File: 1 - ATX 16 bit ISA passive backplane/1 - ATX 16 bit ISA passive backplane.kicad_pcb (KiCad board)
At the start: 2 copper layers, 161.3 x 181.6 mm, 106 parts, among them J1 BUS 1, J10 AB15, J11 AB15, J12 AB15, J13 AB15, J14 AB15, J15 AB15, J16 AB15, J17 3.3V BYPASS, J18 ATX POWER, J19 -5V BYPASS, J2 BUS 2, J20 PWR SW, J21 RST POL, J22 ACT LED, J23 RST SW, J24 RST LED, J25 PWR LED, J3 BUS 3, J4 BUS 4, J5 BUS 5, J6 BUS 6, J7 BUS 7, J8 BREADBOARD HEADER (RC2014 COM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, J9 EXTENDED HEADER, SW1 POWER, SW2 RESET, U1 74HCT14, U2 LM7905, U3 74HCT74

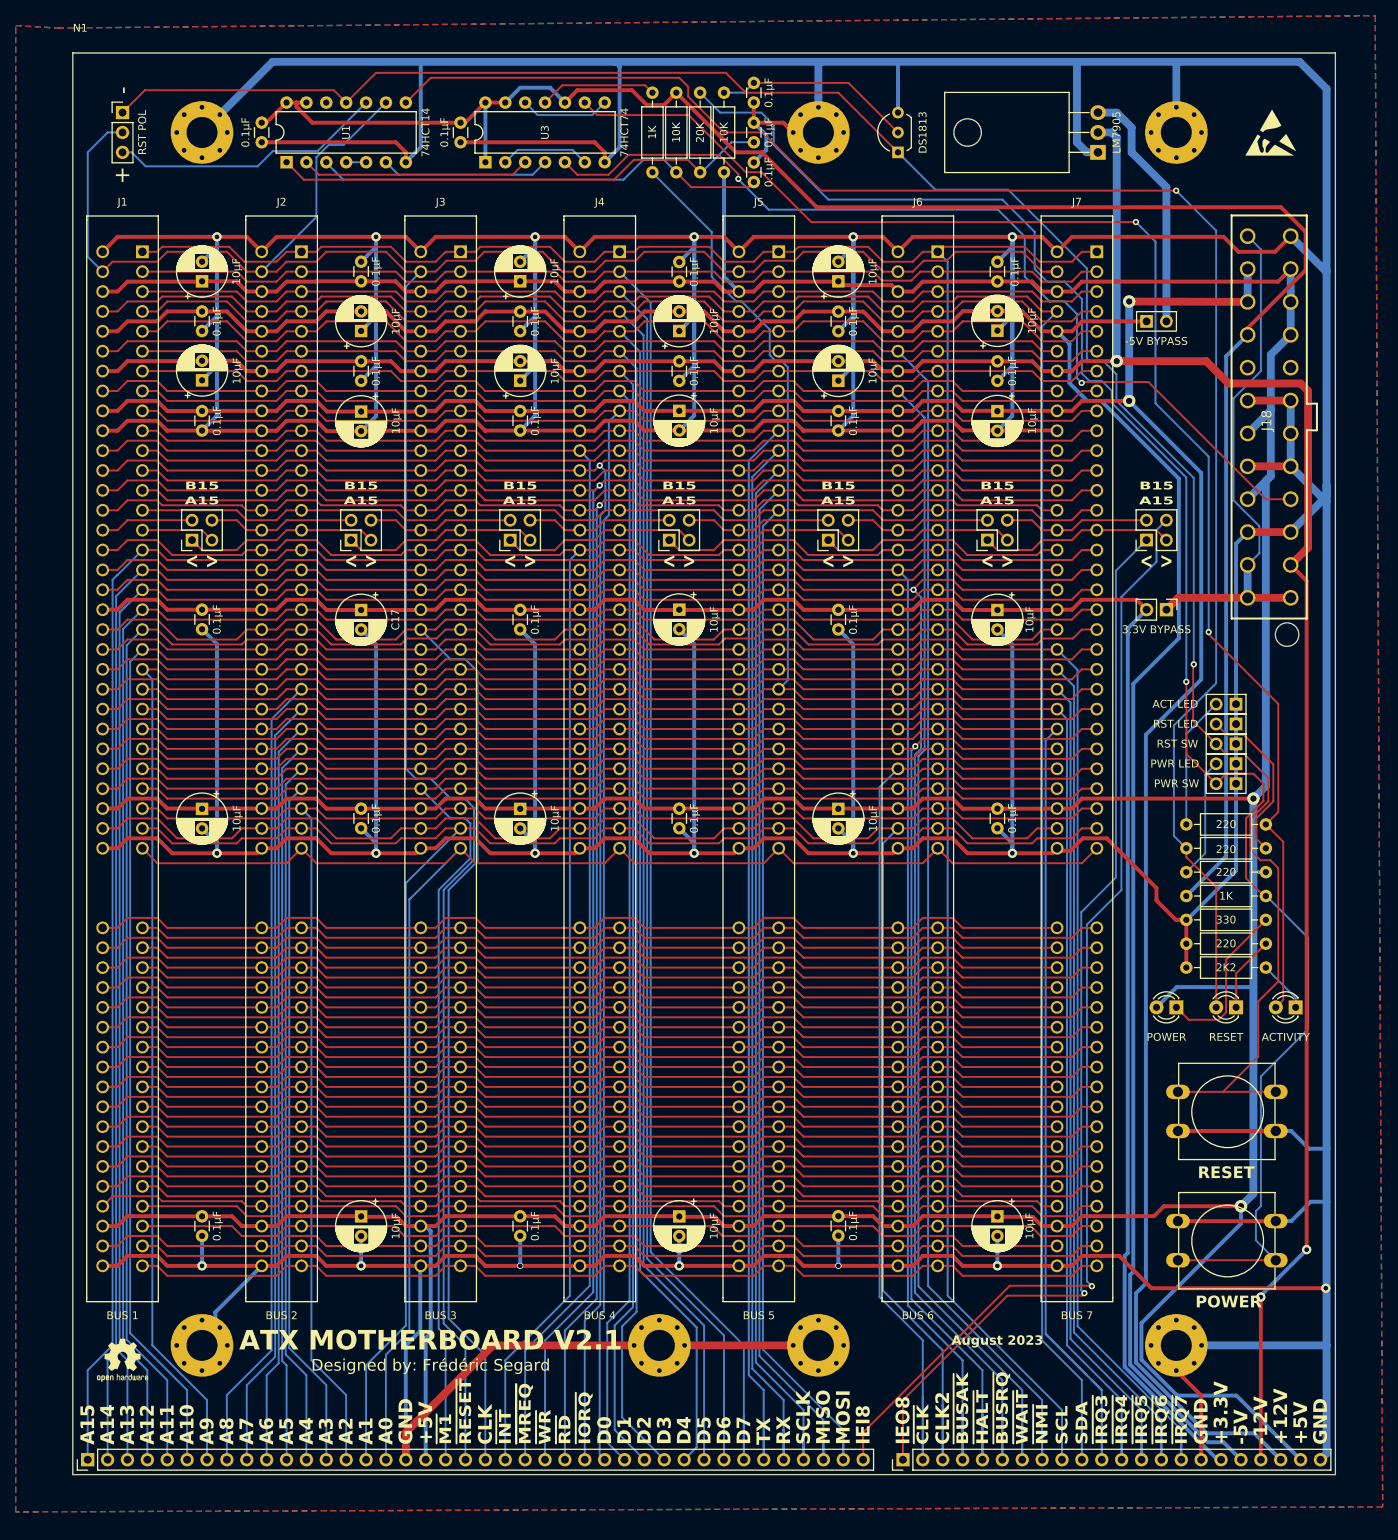
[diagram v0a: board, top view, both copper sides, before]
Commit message: Updated disk activity circuit in mother board, and improved layout in CPU card
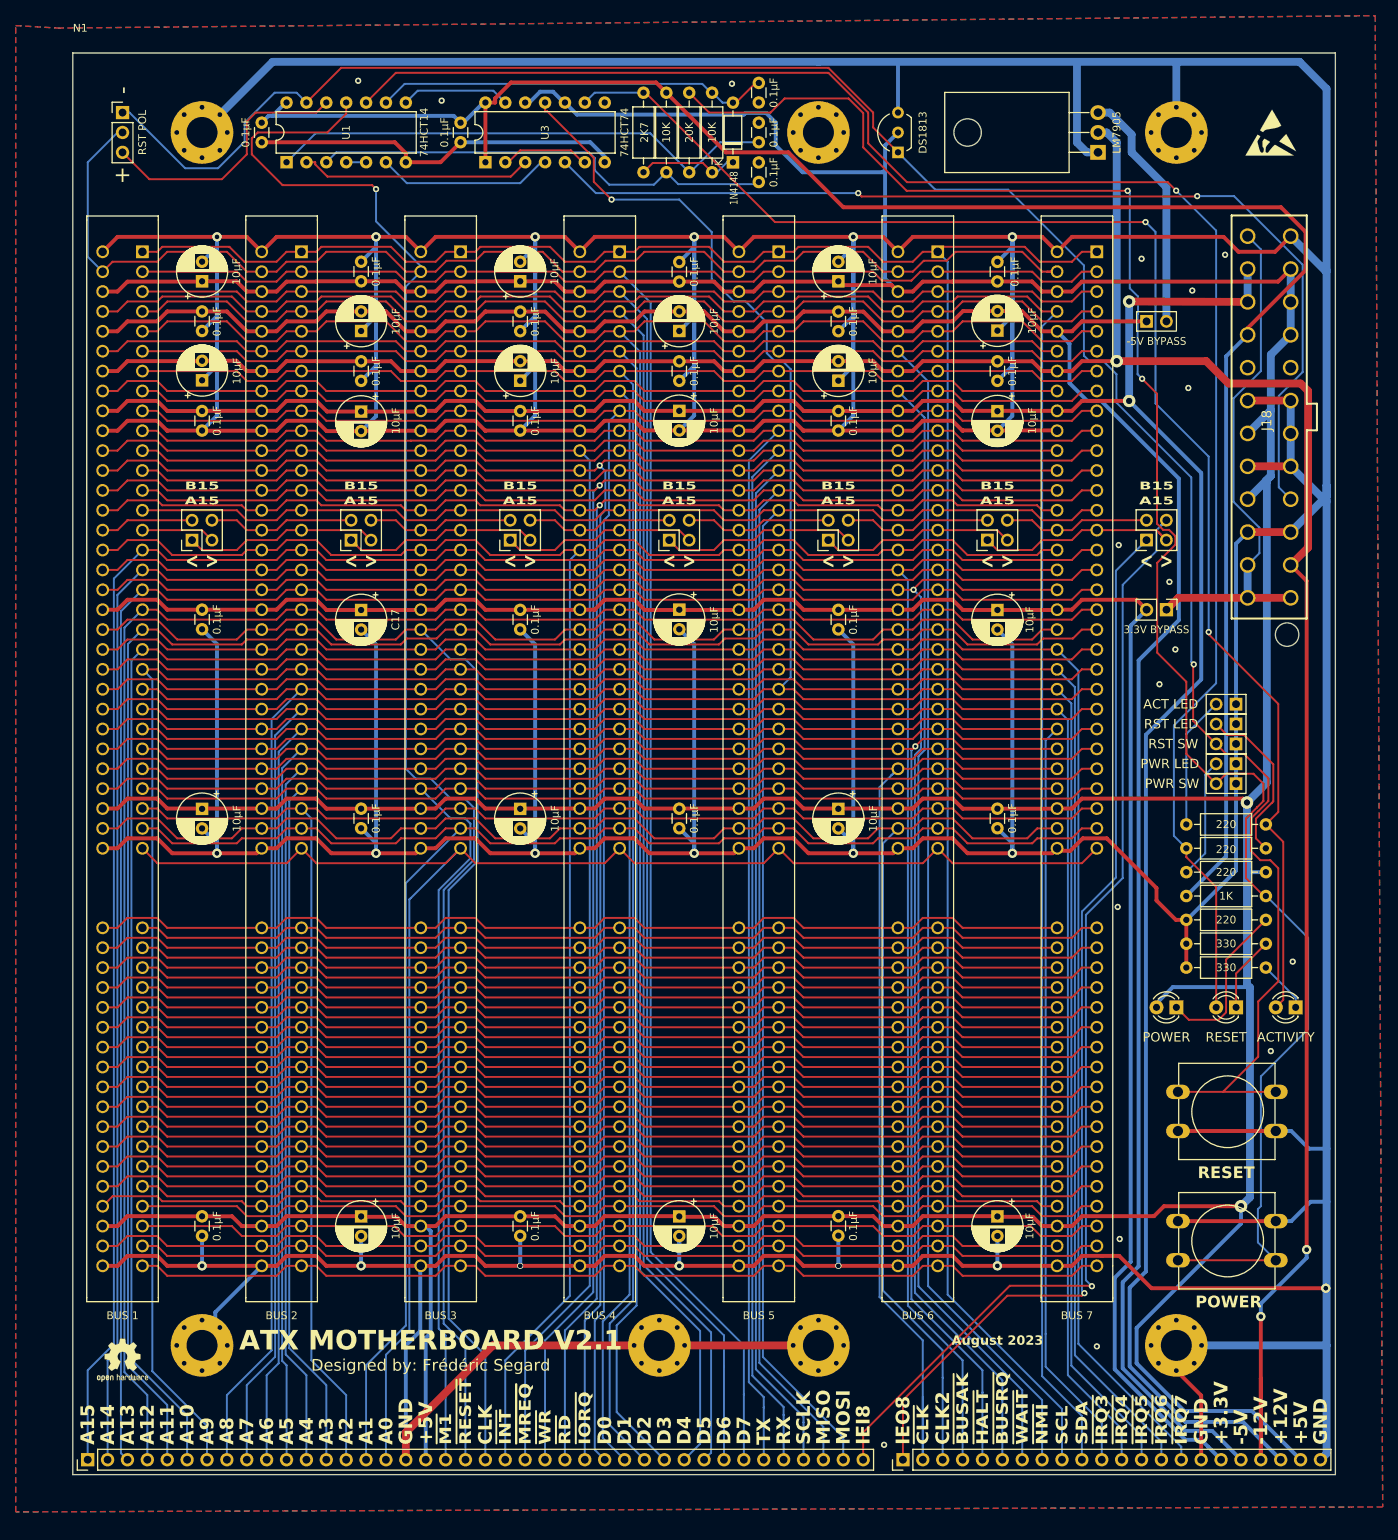
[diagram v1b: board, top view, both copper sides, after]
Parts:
- added D4: 1N4148, Diode_THT:D_DO-35_SOD27_P7.62mm_Horizontal, F.Cu at (104.0, 29.2)
- R11: value 330 -> 220
- R4: value 1K -> 2K7
- R7: value 2K2 -> 330
- R9: value 220 -> 330
- moved R4 10.2 mm to (92.6, 30.5), turned to 90 degrees
- moved R5 1.52 mm to (101.3, 30.5)
- moved R3 1.40 mm to (98.4, 20.3)
- moved R1 1.27 mm to (95.5, 20.3)
- moved C3 0.63 mm to (107.3, 31.7)
- moved C4 0.63 mm to (107.3, 26.6)
- moved C47 0.63 mm to (107.3, 19.1)
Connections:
- C47 pad 1: Net-(RS1-VCC) -> Net-(D4-A)
- R4 pad 1: Net-(U3B-C) -> Net-(D4-K)
- R4 pad 2: /A8 -> Net-(D1-A)
- R5 pad 1: +5V -> Net-(D4-K)
- R5 pad 2: Net-(RS1-VCC) -> Net-(D4-A)
- RS1 pad 2: Net-(RS1-VCC) -> +5V
- U1 pad 10: /Reset & LEDs/+RST -> Net-(D2-A)
- U1 pad 11: /Reset & LEDs/-RST -> /~{RESET}
- U1 pad 12: unconnected-(U1-Pad12) -> /Reset & LEDs/+RST
- U1 pad 13: VCC -> /Reset & LEDs/-RST
- U1 pad 8: Net-(D2-A) -> Net-(U3B-~{R})
- U1 pad 9: /~{RESET} -> Net-(D4-A)
- U3 pad 10: VCC -> +5V
- U3 pad 11: Net-(U3B-C) -> /A8
- U3 pad 12: Net-(U3B-D) -> +5V
- U3 pad 13: VCC -> Net-(U3B-~{R})
- U3 pad 8: Net-(U3B-D) -> unconnected-(U3B-~{Q}-Pad8)
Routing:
- net GND: track 2077.0 -> 2009.8 mm, vias 19 -> 36
- net +5V: track 709.7 -> 770.6 mm
- net Net-(D4-A): track 0.00 -> 50.7 mm
- net Net-(RS1-VCC): track 25.4 -> 0.00 mm
- net /A8: track 305.2 -> 325.9 mm, vias 0 -> 1
- net /~{RESET}: track 347.6 -> 365.0 mm, vias 0 -> 1
- net Net-(U3B-C): track 15.0 -> 0.00 mm
- net Net-(U3B-~{R}): track 0.00 -> 14.0 mm
- net Net-(J20-Pin_2): track 222.6 -> 236.6 mm, vias 1 -> 2
- net /~{IRQ3}: track 238.9 -> 225.2 mm
- net Net-(D4-K): track 0.00 -> 12.9 mm
- net Net-(U3B-D): track 11.5 -> 0.00 mm
- net /Power/~{PS_ON}: track 120.9 -> 131.5 mm
- net -12V: track 334.4 -> 344.4 mm
- net /Reset & LEDs/-RST: track 272.7 -> 281.4 mm
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
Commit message: Trying to hash out the flaws
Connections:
- J1 pad 63: /~{BANK} -> /TX2
- J1 pad 72: /CTCLK -> /RX2
- J1 pad 95: /TX2 -> /USR7
- J1 pad 97: /RX2 -> /USR8
- J2 pad 63: /~{BANK} -> /TX2
- J2 pad 72: /CTCLK -> /RX2
- J2 pad 95: /TX2 -> /USR7
- J2 pad 97: /RX2 -> /USR8
- J3 pad 63: /~{BANK} -> /TX2
- J3 pad 72: /CTCLK -> /RX2
- J3 pad 95: /TX2 -> /USR7
- J3 pad 97: /RX2 -> /USR8
- J4 pad 63: /~{BANK} -> /TX2
- J4 pad 72: /CTCLK -> /RX2
- J4 pad 95: /TX2 -> /USR7
- J4 pad 97: /RX2 -> /USR8
- J5 pad 63: /~{BANK} -> /TX2
- J5 pad 72: /CTCLK -> /RX2
- J5 pad 95: /TX2 -> /USR7
- J5 pad 97: /RX2 -> /USR8
- J6 pad 63: /~{BANK} -> /TX2
- J6 pad 72: /CTCLK -> /RX2
- J6 pad 95: /TX2 -> /USR7
- J6 pad 97: /RX2 -> /USR8
- J7 pad 63: /~{BANK} -> /TX2
- J7 pad 72: /CTCLK -> /RX2
- J7 pad 95: /TX2 -> /USR7
- J7 pad 97: /RX2 -> /USR8
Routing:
- net /USR7: track 0.00 -> 128.2 mm
- net /~{BANK}: track 128.2 -> 0.00 mm
- net /CTCLK: track 128.2 -> 0.00 mm
- net /USR8: track 0.00 -> 128.2 mm

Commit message: Finally finalized the backplane to my liking.
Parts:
- removed the C1 at (43.8, 24.1)
- removed the C11 at (56.5, 50.8)
- removed the C12 at (36.2, 48.3)
- removed the C2 at (69.2, 24.1)
- removed the C25 at (97.2, 50.8)
- removed the C26 at (76.8, 48.3)
- removed the C3 at (107.3, 31.7)
- removed the C4 at (107.3, 26.6)
- removed C40, C47: 0.1µF, Capacitor_THT:C_Disc_D3.0mm_W1.6mm_P2.50mm
- removed D1: ACTIVITY, LED_THT:LED_D3.0mm
- removed D4: 1N4148, Diode_THT:D_DO-35_SOD27_P7.62mm_Horizontal
- removed J11: AB15, 0_Library:PinHeader_2x2_Vertical (Modified)
- removed J22: ACT LED, 0_Library:PinHeader_1x2_Vertical (Modified)
- removed J23: RST SW, 0_Library:PinHeader_1x2_Vertical (Modified)
- removed J24: RST LED, 0_Library:PinHeader_1x2_Vertical (Modified)
- removed J25: PWR LED, 0_Library:PinHeader_1x2_Vertical (Modified)
- removed the J8 at (21.6, 194.9)
- removed the J9 at (125.7, 194.9)
- removed the LOGO1 at (81.9, 184.2)
- removed LOGO3: Logo_Open_Hardware_Small, 0_Library:JLCPCB Logo 3
- removed LOGO4, LOGO6: Logo_Open_Hardware_Small, Symbol:ESD-Logo_6.6x6mm_SilkScreen
- added C37: 10µF, Capacitor_THT:CP_Radial_D6.3mm_P2.50mm, F.Cu at (162.5, 38.1)
- added C38: 1µF, Capacitor_THT:C_Disc_D3.0mm_W1.6mm_P2.50mm, F.Cu at (37.4, 35.7)
- added C41: 22µF, Capacitor_THT:C_Disc_D3.0mm_W1.6mm_P2.50mm, F.Cu at (128.9, 26.7)
- added C42: 1µF, Capacitor_THT:C_Disc_D3.0mm_W1.6mm_P2.50mm, F.Cu at (161.2, 48.3)
- added C44: 1µF, Capacitor_THT:C_Disc_D3.0mm_W1.6mm_P2.50mm, F.Cu at (42.5, 22.9)
- added C45: 1µF, Capacitor_THT:C_Disc_D3.0mm_W1.6mm_P2.50mm, F.Cu at (64.1, 22.9)
- added C46: 1µF, Capacitor_THT:C_Disc_D3.0mm_W1.6mm_P2.50mm, F.Cu at (75.6, 35.6)
- added J2: A: Component Side, Connector_PinHeader_2.54mm:PinHeader_1x31_P2.54mm_Vertical, F.Cu at (21.6, 194.9)
- added J3: B: Back Side, Connector_PinHeader_2.54mm:PinHeader_1x31_P2.54mm_Vertical, F.Cu at (102.9, 194.9)
- added Q1: IRF4905PBF, Package_TO_SOT_THT:TO-220-3_Horizontal_TabDown, F.Cu at (152.2, 27.9)
- added Q2: 2N3904, Package_TO_SOT_THT:TO-92_Inline_Wide, F.Cu at (121.3, 22.5)
- added Q3: 2N3904, Package_TO_SOT_THT:TO-92_Inline_Wide, F.Cu at (121.3, 28.3)
- added R14: 10K, Resistor_THT:R_Axial_DIN0207_L6.3mm_D2.5mm_P10.16mm_Horizontal, F.Cu at (70.5, 31.8)
- added R15: 2K7, Resistor_THT:R_Axial_DIN0207_L6.3mm_D2.5mm_P10.16mm_Horizontal, F.Cu at (55.9, 31.8)
- added R16: 2K2, Resistor_THT:R_Axial_DIN0207_L6.3mm_D2.5mm_P10.16mm_Horizontal, F.Cu at (175.0, 135.9)
- added R17: 220, Resistor_THT:R_Axial_DIN0207_L6.3mm_D2.5mm_P10.16mm_Horizontal, F.Cu at (171.8, 135.9)
- added U4: LM7905, Package_TO_SOT_THT:TO-220-3_Horizontal_TabDown, F.Cu at (163.8, 83.7)
- added locked: PWR IN SEL, Connector_PinHeader_2.54mm:PinHeader_2x03_P2.54mm_Vertical, F.Cu at (172.1, 38.7)
- C12: renamed from C46; value 0.1µF -> 1µF
- C16: renamed from C8; value 0.1µF -> 1µF
- C17: renamed from C22; value 0.1µF -> 1µF
- C18: renamed from C36; value 0.1µF -> 1µF
- C20: renamed from C14; value 0.1µF -> 1µF
- C21: renamed from C9; value 0.1µF -> 1µF
- C22: renamed from C23; value 0.1µF -> 1µF
- C23: renamed from C37; value 0.1µF -> 1µF
- C25: renamed from C28; value 0.1µF -> 1µF
- C26: renamed from C10; value 0.1µF -> 1µF
- C27: renamed from C24; value 0.1µF -> 1µF
- C28: renamed from C38; value 0.1µF -> 1µF
- C30: renamed from C42; value 0.1µF -> 1µF
- C32: renamed from C16; value 0.1µF -> 1µF
- C34: renamed from C30; value 0.1µF -> 1µF
- C36: renamed from C44; value 0.1µF -> 1µF
- C39: value 10µF -> 1µF; footprint Capacitor_THT:CP_Radial_D6.3mm_P2.50mm -> Capacitor_THT:C_Disc_D3.0mm_W1.6mm_P2.50mm
- C5: renamed from C18; value 0.1µF -> 1µF
- C7: renamed from C32; value 0.1µF -> 1µF
- D2: value RESET -> 1N4148; footprint LED_THT:LED_D3.0mm -> Diode_THT:D_DO-35_SOD27_P7.62mm_Horizontal
- D3: value POWER -> ACTIVITY
- J10: value AB15 -> ATX POWER; footprint 0_Library:PinHeader_2x2_Vertical (Modified) -> 0_Library:ATX_PSU_CONN
- J12: value AB15 -> PWR SW SEL; footprint 0_Library:PinHeader_2x2_Vertical (Modified) -> Connector_PinHeader_2.54mm:PinHeader_2x03_P2.54mm_Vertical
- J13: value AB15 -> PWR_LED; footprint 0_Library:PinHeader_2x2_Vertical (Modified) -> 0_Library:PinHeader_1x2_Vertical (Modified)
- J14: value AB15 -> PWR_SW; footprint 0_Library:PinHeader_2x2_Vertical (Modified) -> 0_Library:PinHeader_1x2_Vertical (Modified)
- J15: value AB15 -> 5V DC (CP); footprint 0_Library:PinHeader_2x2_Vertical (Modified) -> Connector_BarrelJack:BarrelJack_Horizontal
- J16: value AB15 -> RST POLARITY; footprint 0_Library:PinHeader_2x2_Vertical (Modified) -> Connector_PinHeader_2.54mm:PinHeader_1x03_P2.54mm_Vertical
- J17: value 3.3V BYPASS -> RST_LED; footprint Connector_PinHeader_2.54mm:PinHeader_1x02_P2.54mm_Vertical -> 0_Library:PinHeader_1x2_Vertical (Modified)
- J18: value ATX POWER -> RST_SW; footprint 0_Library:ATX_PSU_CONN -> 0_Library:PinHeader_1x2_Vertical (Modified)
- J19: value -5V BYPASS -> 3V/-5V; footprint 0_Library:PinHeader_1x2_Vertical (Modified) -> Connector_PinHeader_2.54mm:PinHeader_1x03_P2.54mm_Vertical
- J20: value PWR SW -> ACT LED
- J21: value RST POL -> ACTIVITY ADDR
- R1: value 10K -> 220
- R10: value 220 -> 330
- R2: value 1K -> 220
- R3: value 20K -> 100K
- R4: value 2K7 -> 10K
- R5: value 10K -> 1K
- R6: value 220 -> 100K
- R7: value 330 -> 100K
- R8: value 220 -> 1K
- R9: value 330 -> 20K
- SW1, SW2: footprint Button_Switch_THT:SW_PUSH-12mm -> 0_Library:Pushbutton_12mm_LED
- U2: value LM7905 -> LD1117V33
- moved J10 143.5 mm to (178.4, 77.4)
- moved J16 142.0 mm to (23.5, 28.6)
- moved D2 140.8 mm to (74.9, 31.8), turned to 0 degrees
- moved R1 131.9 mm to (159.1, 135.9), turned to 90 degrees
- moved R7 130.8 mm to (104.1, 20.3), turned to -90 degrees
- moved R9 129.4 mm to (88.3, 30.5), turned to 90 degrees
- moved R8 125.8 mm to (91.4, 20.3), turned to -90 degrees
- moved R6 117.5 mm to (101.0, 20.3), turned to -90 degrees
- moved C39 102.0 mm to (37.4, 32.5), turned to 180 degrees
- moved RS1 101.8 mm to (23.5, 22.3), turned to 0 degrees
- moved J21 92.6 mm to (76.8, 100.3), turned to 180 degrees
- moved J12 91.6 mm to (160.3, 112.3), turned to 0 degrees
- moved J13 83.1 mm to (168.8, 117.3)
- moved J14 69.6 mm to (171.3, 119.9), turned to -90 degrees
- moved J15 61.9 mm to (175.6, 29.5), turned to -90 degrees
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- renumbered C5 to C1, C34 to C10, C45 to C11, C7 to C13, C21 to C14, C35 to C15, C13 to C19, C19 to C2, C27 to C24, C41 to C29, C33 to C3, C15 to C31, C29 to C33, C43 to C35, C17 to C4, C31 to C6, C6 to C8, C20 to C9, J2 to J4, J3 to J5, J4 to J6, J5 to J7, J6 to J8, J7 to J9, LOGO2 to LOGO1, LOGO5 to LOGO2
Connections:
- C39 pad 1: GND -> Net-(C39-Pad1)
- C39 pad 2: -5V -> GND
- D3 pad 2: +5V -> Net-(D3-A)
- J1 pad 1: /SCL -> /TX
- J1 pad 10: /TX -> /RX
- J1 pad 11: /RX -> /MOSI
- J1 pad 12: /SCLK -> /MISO
- J1 pad 13: /MISO -> /SCLK
- J1 pad 14: /MOSI -> /SDA
- J1 pad 15: /IEO1 -> /SCL
- J1 pad 35: /SDA -> /~{IRQ2}
- J1 pad 36: -5V -> +3V3
- J1 pad 37: /~{NMI} -> /~{M1}
- J1 pad 39: /~{WAIT} -> /CLK2
- J1 pad 46: /IEI1 -> /~{BUSRQ}
- J1 pad 47: /~{INT} -> /~{BUSAK}
- J1 pad 48: /~{BUSAK} -> /~{WAIT}
- J1 pad 49: /~{BUSRQ} -> /~{HALT}
- J1 pad 50: +3V3 -> /~{RFSH}
- J1 pad 57: /~{HALT} -> /~{NMI}
- J1 pad 58: /~{CLK} -> /CTCLK1
- J1 pad 59: /~{M1} -> /CTCLK2
- J1 pad 61: /CLK2 -> /~{CLK}
- J10 pad 1: /IEO2 -> /Power/ATX_3V3
- J10 pad 2: /IEI1 -> /Power/ATX_3V3
- J10 pad 3: /IEO1 -> GND
- J10 pad 4: /IEI2 -> /Power/ATX_5V
- J12 pad 1: /IEO4 -> /Power/ALT1
- J12 pad 2: /IEI3 -> /Power/ALT2
- J12 pad 3: /IEO3 -> Net-(J12-Pin_3)
- J12 pad 4: /IEI4 -> Net-(J12-Pin_4)
- J13 pad 1: /IEO5 -> Net-(J13-Pin_1)
- J13 pad 2: /IEI4 -> GND
- J14 pad 1: /IEO6 -> Net-(J12-Pin_4)
- J14 pad 2: /IEI5 -> Net-(J12-Pin_3)
- J15 pad 1: /IEO7 -> /Power/Vin
- J15 pad 2: /IEI6 -> GND
- J15 pad 3: /IEO6 -> GND
- J16 pad 1: /IEO8 -> /Reset & LEDs/-RST
- J16 pad 2: /IEI7 -> /~{RESET}
- J16 pad 3: /IEO7 -> /Reset & LEDs/+RST
- J17 pad 1: /Power/3V3 -> Net-(J17-Pin_1)
- J17 pad 2: +3V3 -> GND
- J18 pad 1: /Power/3V3 -> GND
- J18 pad 2: /Power/3V3 -> /Reset & LEDs/-RST
- J19 pad 1: -5V -> /Power/ATX_3V3
- J19 pad 2: Net-(J19-Pin_2) -> +3V3
- J21 pad 1: /Reset & LEDs/-RST -> /A7
- J21 pad 2: /~{RESET} -> Net-(J21-Pin_2)
- J21 pad 3: /Reset & LEDs/+RST -> /A8
- J4 pad 1: /SCL -> /TX
- J4 pad 10: /TX -> /RX
- J4 pad 11: /RX -> /MOSI
- J4 pad 12: /SCLK -> /MISO
- J4 pad 13: /MISO -> /SCLK
- J4 pad 14: /MOSI -> /SDA
- J4 pad 15: /IEO2 -> /SCL
- J4 pad 35: /SDA -> /~{IRQ2}
- J4 pad 36: -5V -> +3V3
- J4 pad 37: /~{NMI} -> /~{M1}
- J4 pad 39: /~{WAIT} -> /CLK2
- J4 pad 46: /IEI2 -> /~{BUSRQ}
- J4 pad 47: /~{INT} -> /~{BUSAK}
- J4 pad 48: /~{BUSAK} -> /~{WAIT}
- J4 pad 49: /~{BUSRQ} -> /~{HALT}
- J4 pad 50: +3V3 -> /~{RFSH}
- J4 pad 57: /~{HALT} -> /~{NMI}
- J4 pad 58: /~{CLK} -> /CTCLK1
- J4 pad 59: /~{M1} -> /CTCLK2
- J4 pad 61: /CLK2 -> /~{CLK}
- J5 pad 1: /SCL -> /TX
- J5 pad 10: /TX -> /RX
- J5 pad 11: /RX -> /MOSI
- J5 pad 12: /SCLK -> /MISO
- J5 pad 13: /MISO -> /SCLK
- J5 pad 14: /MOSI -> /SDA
- J5 pad 15: /IEO3 -> /SCL
- J5 pad 35: /SDA -> /~{IRQ2}
- J5 pad 36: -5V -> +3V3
- J5 pad 37: /~{NMI} -> /~{M1}
- J5 pad 39: /~{WAIT} -> /CLK2
- J5 pad 46: /IEI3 -> /~{BUSRQ}
- J5 pad 47: /~{INT} -> /~{BUSAK}
- J5 pad 48: /~{BUSAK} -> /~{WAIT}
- J5 pad 49: /~{BUSRQ} -> /~{HALT}
- J5 pad 50: +3V3 -> /~{RFSH}
- J5 pad 57: /~{HALT} -> /~{NMI}
- J5 pad 58: /~{CLK} -> /CTCLK1
- J5 pad 59: /~{M1} -> /CTCLK2
- J5 pad 61: /CLK2 -> /~{CLK}
- J6 pad 1: /SCL -> /TX
- J6 pad 10: /TX -> /RX
- J6 pad 11: /RX -> /MOSI
- J6 pad 12: /SCLK -> /MISO
- J6 pad 13: /MISO -> /SCLK
- J6 pad 14: /MOSI -> /SDA
- J6 pad 15: /IEO4 -> /SCL
- J6 pad 35: /SDA -> /~{IRQ2}
- J6 pad 36: -5V -> +3V3
- J6 pad 37: /~{NMI} -> /~{M1}
- J6 pad 39: /~{WAIT} -> /CLK2
- J6 pad 46: /IEI4 -> /~{BUSRQ}
- J6 pad 47: /~{INT} -> /~{BUSAK}
- J6 pad 48: /~{BUSAK} -> /~{WAIT}
- J6 pad 49: /~{BUSRQ} -> /~{HALT}
- J6 pad 50: +3V3 -> /~{RFSH}
- J6 pad 57: /~{HALT} -> /~{NMI}
- J6 pad 58: /~{CLK} -> /CTCLK1
- J6 pad 59: /~{M1} -> /CTCLK2
- J6 pad 61: /CLK2 -> /~{CLK}
- J7 pad 1: /SCL -> /TX
- J7 pad 10: /TX -> /RX
- J7 pad 11: /RX -> /MOSI
- J7 pad 12: /SCLK -> /MISO
- J7 pad 13: /MISO -> /SCLK
- J7 pad 14: /MOSI -> /SDA
- J7 pad 15: /IEO5 -> /SCL
- J7 pad 35: /SDA -> /~{IRQ2}
- J7 pad 36: -5V -> +3V3
- J7 pad 37: /~{NMI} -> /~{M1}
- J7 pad 39: /~{WAIT} -> /CLK2
- J7 pad 46: /IEI5 -> /~{BUSRQ}
- J7 pad 47: /~{INT} -> /~{BUSAK}
- J7 pad 48: /~{BUSAK} -> /~{WAIT}
- J7 pad 49: /~{BUSRQ} -> /~{HALT}
- J7 pad 50: +3V3 -> /~{RFSH}
- J7 pad 57: /~{HALT} -> /~{NMI}
- J7 pad 58: /~{CLK} -> /CTCLK1
- J7 pad 59: /~{M1} -> /CTCLK2
- J7 pad 61: /CLK2 -> /~{CLK}
- J8 pad 1: /SCL -> /TX
- J8 pad 10: /TX -> /RX
- J8 pad 11: /RX -> /MOSI
- J8 pad 12: /SCLK -> /MISO
- J8 pad 13: /MISO -> /SCLK
- J8 pad 14: /MOSI -> /SDA
- J8 pad 15: /IEO6 -> /SCL
- J8 pad 35: /SDA -> /~{IRQ2}
- J8 pad 36: -5V -> +3V3
- J8 pad 37: /~{NMI} -> /~{M1}
- J8 pad 39: /~{WAIT} -> /CLK2
- J8 pad 46: /IEI6 -> /~{BUSRQ}
- J8 pad 47: /~{INT} -> /~{BUSAK}
- J8 pad 48: /~{BUSAK} -> /~{WAIT}
- J8 pad 49: /~{BUSRQ} -> /~{HALT}
- J8 pad 50: +3V3 -> /~{RFSH}
- J8 pad 57: /~{HALT} -> /~{NMI}
- J8 pad 58: /~{CLK} -> /CTCLK1
- J8 pad 59: /~{M1} -> /CTCLK2
- J8 pad 61: /CLK2 -> /~{CLK}
- J9 pad 1: /SCL -> /TX
- J9 pad 10: /TX -> /RX
- J9 pad 11: /RX -> /MOSI
- J9 pad 12: /SCLK -> /MISO
- J9 pad 13: /MISO -> /SCLK
- J9 pad 14: /MOSI -> /SDA
- J9 pad 15: /IEO7 -> /SCL
- J9 pad 35: /SDA -> /~{IRQ2}
- J9 pad 36: -5V -> +3V3
- J9 pad 37: /~{NMI} -> /~{M1}
- J9 pad 39: /~{WAIT} -> /CLK2
- J9 pad 46: /IEI7 -> /~{BUSRQ}
- J9 pad 47: /~{INT} -> /~{BUSAK}
- J9 pad 48: /~{BUSAK} -> /~{WAIT}
- J9 pad 49: /~{BUSRQ} -> /~{HALT}
- J9 pad 50: +3V3 -> /~{RFSH}
- J9 pad 57: /~{HALT} -> /~{NMI}
- J9 pad 58: /~{CLK} -> /CTCLK1
- J9 pad 59: /~{M1} -> /CTCLK2
- J9 pad 61: /CLK2 -> /~{CLK}
- R1 pad 1: VCC -> Net-(SW1-A)
- R1 pad 2: Net-(C3-Pad1) -> +5V
- R10 pad 1: Net-(J25-Pin_2) -> Net-(SW2-A)
- R10 pad 2: +5V -> Net-(R10-Pad2)
- R11 pad 1: Net-(D3-K) -> Net-(J17-Pin_1)
- R11 pad 2: GND -> Net-(R10-Pad2)
- R2 pad 1: VCC -> Net-(J13-Pin_1)
- R2 pad 2: Net-(J20-Pin_2) -> +5V
- R3 pad 1: Net-(J20-Pin_2) -> Net-(Q1-G)
- R3 pad 2: Net-(C4-Pad1) -> /Power/Vin
- R4 pad 1: Net-(D4-K) -> VCC
- R4 pad 2: Net-(D1-A) -> Net-(C38-Pad1)
- R5 pad 1: Net-(D4-K) -> GND
- R5 pad 2: Net-(D4-A) -> Net-(Q2-E)
- R6 pad 1: Net-(D1-A) -> /Power/ALT1
- R6 pad 2: Net-(J22-Pin_2) -> /Power/ALT_5V
- R7 pad 1: Net-(D1-K) -> /Power/ALT2
- R7 pad 2: GND -> /Power/Vin
- R8 pad 1: Net-(J24-Pin_2) -> VCC
- R8 pad 2: Net-(D2-A) -> /Power/ATX
- R9 pad 1: Net-(D2-K) -> /Power/ATX
- R9 pad 2: GND -> Net-(C39-Pad1)
- SW1 pad 1: GND -> Net-(J12-Pin_4)
- SW1 pad 2: Net-(J20-Pin_2) -> Net-(J12-Pin_3)
- SW2 pad 1: /Reset & LEDs/-RST -> GND
- SW2 pad 2: GND -> /Reset & LEDs/-RST
- U1 pad 1: Net-(C4-Pad1) -> Net-(C39-Pad1)
- U1 pad 10: Net-(D2-A) -> Net-(R10-Pad2)
- U1 pad 3: Net-(C3-Pad1) -> Net-(C38-Pad1)
- U1 pad 9: Net-(D4-A) -> Net-(D2-A)
- U2 pad 2: -12V -> /Power/ALT_3V3
- U2 pad 3: Net-(J19-Pin_2) -> /Power/ALT_5V
- U3 pad 11: /A8 -> Net-(J21-Pin_2)
- U3 pad 9: Net-(D1-A) -> Net-(D3-A)
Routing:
- net -5V: track 309.4 -> 0.00 mm
- net /~{IRQ2}: track 0.00 -> 297.2 mm
- net Net-(D3-A): track 0.00 -> 264.2 mm, vias 0 -> 2
- net GND: track 2009.8 -> 1748.3 mm, vias 36 -> 35
- net /~{RFSH}: track 0.00 -> 254.7 mm
- net /~{INT}: track 251.5 -> 0.00 mm
- net /CTCLK1: track 0.00 -> 248.6 mm
- net /CTCLK2: track 0.00 -> 247.8 mm
- net Net-(J20-Pin_2): track 236.6 -> 18.7 mm, vias 2 -> 0
- net Net-(R10-Pad2): track 0.00 -> 188.6 mm, vias 0 -> 2
- net Net-(D1-A): track 188.3 -> 0.00 mm, vias 2 -> 0
- net Net-(D2-A): track 224.5 -> 39.2 mm, vias 1 -> 0
- net /Power/ATX: track 0.00 -> 151.5 mm
- net /IEI8: track 143.8 -> 0.00 mm, vias 1 -> 0
- net /Power/ALT2: track 0.00 -> 143.6 mm, vias 0 -> 1
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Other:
- board text added: "16-BIT ISA PASSIVE ATX BACKPLANE"
- board text added: "3.3V"
- board text added: "3V"
- board text added: "A01"
- board text added: "A02"
- board text added: "A03"
- board text added: "A04"
- board text added: "A05"
- board text added: "A06"
- board text added: "A07"
- board text added: "A08"
- board text added: "A09"
- board text added: "A16"
- board text added: "A17"
- board text added: "A18"
- board text added: "A19"
- board text added: "A20"
- board text added: "A21"
- board text added: "A22"
- board text added: "A23"
- board text added: "A24"
- board text added: "A25"
- board text added: "A26"
- board text added: "A27"
- board text added: "A28"
- board text added: "A29"
- board text added: "A30"
- board text added: "A31"
- board text added: "AEN"
- board text added: "ALE"
- board text added: "ALT"
- board text added: "ALT 3V3"
- board text added: "ALT 5V"
- board text added: "ATX"
- board text added: "ATX 3V3"
- board text added: "ATX 5V"
- board text added: "B01"
- board text added: "B02"
- board text added: "B03"
- board text added: "B04"
- board text added: "B05"
- board text added: "B06"
- board text added: "B07"
- board text added: "B08"
- board text added: "B09"
- board text added: "B10"
- board text added: "B11"
- board text added: "B12"
- board text added: "B13"
- board text added: "B14"
- board text added: "B16"
- board text added: "B17"
- board text added: "B18"
- board text added: "B19"
- board text added: "B20"
- board text added: "B21"
- board text added: "B22"
- board text added: "B23"
- board text added: "B24"
- board text added: "B25"
- board text added: "B26"
- board text added: "B27"
- board text added: "B28"
- board text added: "B29"
- board text added: "B30"
- board text added: "B31"
- board text added: "BE"
- board text added: "CTCLK1"
- board text added: "CTCLK2"
- board text added: "DRQ1"
- board text added: "DRQ2"
- board text added: "DRQ3"
- board text added: "IOCR"
- board text added: "OSC"
- board text added: "R/~{W}"
- board text added: "RDY"
- board text added: "RESET"
- board text added: "Rev 2.1: September 2023"
- board text added: "SYNC"
- board text added: "T/C"
- board text added: "www.youtube.com/@microhobbyist www.github.com/FredericSegard"
- board text added: "~{DACK1}"
- board text added: "~{DACK2}"
- board text added: "~{DACK3}"
- board text added: "~{INT}*"
- board text added: "~{IOCC}"
- board text added: "~{IOR}"
- board text added: "~{IOW}"
- board text added: "~{IRQ2}"
- board text added: "~{IRQ}*"
- board text added: "~{MEMR}"
- board text added: "~{MEMW}"
- board text added: "~{ML}"
- board text added: "~{NWS}"
- board text added: "~{RFRSH}"
- board text added: "~{SO}"
- board text added: "~{VP}"
- board text added: "Φ1"
- board text added: "Φ2"
- board text removed: "+3.3V"
- board text removed: "<"
- board text removed: ">"
- board text removed: "ATX MOTHERBOARD V2.1"
- board text removed: "IEI8"
- board text removed: "IEO8"
- board text removed: "Made in Canada www.youtube.com/@microhobbyist www.github.com/FredericSegard"
- board text removed: "~{INT}"
